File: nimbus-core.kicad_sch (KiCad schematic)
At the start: 0 parts

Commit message: Import shematic
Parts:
- added C1, C11, C13, C15, C16, C17, C18, C20, C21, C23, C24, C25, C4, C6, C7, C9: 100nF, passive:C_0603_Density_Nominal, symbol passive:C0603C104J3RACAUTO
- added C10, C14: 1μF, passive:C_0805_Density_Nominal, symbol passive:C0805C105J3RECAUTO
- added C12: 10μF, passive:C_0805_Density_Nominal, symbol passive:GCM21BR71A106KE22K
- added C19: 4.7μF, passive:C_1206_Density_Nominal, symbol passive:C1206F475K4RACAUTO
- added C2, C3: 10pF, passive:C_0603_Density_Nominal, symbol passive:C0603C100J1GACAUTO
- added C22, C26: 4.7nF, passive:C_0603_Density_Nominal, symbol passive:C0603C472F5GACAUTO
- added C5, C8: 2.2μF, passive:C_0805_Density_Nominal, symbol passive:C0805C225K4RECAUTO
- added D1, D2, D3, D4: ~, diode:D1213A-01T-7, symbol diode:D1213A-01T-7
- added J1: QTE-020-03-L-D-A, connector:QTE-020-03-L-D-A, symbol connector:QTE-020-03-L-D-A
- added J2: QSE-020-01-L-D-A, connector:QSE-020-01-L-D-A, symbol connector:QSE-020-01-L-D-A
- added J3, J6: 532614006, connector:532614004, symbol connector:532614004
- added J4: USB4105-GF-A-120, connector:USB4105-GF-A-120, symbol connector:USB4105-GF-A-120
- added J5: 532614006, connector:532614006, symbol connector:532614006
- added R1, R10, R11, R17, R18, R2, R5, R6, R7, R8, R9: 10kΩ, passive:R_0603_Density_Nominal, symbol passive:CRCW060310K0FKEAHP
- added R12, R13: 0Ω, passive:R_0603_Density_Nominal, symbol passive:CRCW06030000Z0EA
- added R14, R15, R26, R27: 60.4Ω, passive:R_0603_Density_Nominal, symbol passive:CRCW060360R4FKEAHP
- added R16: 10kΩ, passive:C_0603_Density_Nominal, symbol passive:CRCW060310K0FKEAHP
- added R19, R20: 1.8kΩ, passive:R_0603_Density_Nominal, symbol passive:CRCW06031K80FKEAHP
- added R21: 100Ω, passive:R_0603_Density_Nominal, symbol passive:CRCW0603100RFKEA
- added R22, R25: 5.1kΩ, passive:R_0603_Density_Nominal, symbol passive:CRCW06035K10FKEAHP
- added R23: 82kΩ, passive:R_0603_Density_Nominal, symbol passive:CRCW060382K0FKEA
- added R24: 33kΩ, passive:R_0603_Density_Nominal, symbol passive:CRCW060333K0FKEAHP
- added R3, R4: 22.1Ω, passive:R_0603_Density_Nominal, symbol passive:CRCW060322R1FKEA
- added U1: ${MANUFACTURER PART NUMBER}, ic:STM32F405VGT7, symbol ic:STM32F405VGT7
- added U10: ${COLOR}, diode:TLMY1100-GS15, symbol diode:TLMY1100-GS15
- added U4: SN65HVD233-Q1, ic:SN65HVD233-Q1, symbol ic:SN65HVD233-Q1
- added U8: SN65HVD1782-Q1, ic:SN65HVD1782-Q1, symbol ic:SN65HVD1782-Q1
- added U9: USBLC6-2P6, diode:USBLC6-2P6, symbol diode:USBLC6-2P6
- added Y1: 25MHz, passive:ABM11AIG-25.000MHZ-4Z-T3, symbol passive:ABM11AIG-25.000MHZ-4Z-T3
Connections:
- new net: R3.2, U4.4 (RXD)
- new net: R11.2, R13.1, U4.8 (RS)
- new net: C22.1, R14.2, R15.1
- new net: C26.1, R26.2, R27.1
- new net: R12.2, U4.5 (LBK)
- new net: R4.2, R5.2, U4.1 (TXD)
- new net: R21.2, U10.2
- new net +3.3V: C10.1, C11.1, C12.1, C13.1, C14.1, C15.1, C16.1, C17.1, C18.1, C19.1, C23.1, C4.1, C6.1, C7.1, C9.1, J3.1, J5.1, J6.1, R10.1, R11.1, R16.1, R17.1, R19.1, R2.1, R20.1, R5.1, R6.1, R7.1, R8.1, R9.1, U1.100 (VDD), U1.11 (VDD), U1.19 (VDD), U1.21 (VREF+), U1.22 (VDDA), U1.28 (VDD), U1.50 (VDD), U1.6 (VBAT), U1.75 (VDD), U4.3 (VCC), U8.8 (VCC)
- new net ACCEL_IRQ: U1.40 (PE9)
- new net BOOT0: R1.1, U1.94 (BOOT0)
- new net BUZZER: U1.77 (PA15)
- new net CAN1_RX: R3.1, U1.81 (PD0)
- new net CAN1_TX: R4.1, U1.82 (PD1)
- new net CAN_N: C20.1, J3.2, R15.2, U4.6 (CANL)
- new net CAN_P: C21.1, J3.3, R14.1, U4.7 (CANH)
- new net CC1: J4.A5 (CC1), R22.1
- new net CC2: J4.B5 (CC2), R25.1
- new net CHASSIS: J3.MP, J4.SH, J5.MP, J6.MP
- new net FIRE_PYRO1: U1.87 (PD6)
- new net FIRE_PYRO2: U1.86 (PD5)
- new net GND: C1.2, C10.2, C11.2, C12.2, C13.2, C14.2, C15.2, C16.2, C17.2, C18.2, C19.2, C2.2, C20.2, C21.2, C22.2, C23.2, C24.2, C25.2, C26.2, C3.2, C4.2, C5.2, C6.2, C7.2, C8.2, C9.2, D1.2, D2.2, D3.2, D4.2, J1.G1, J1.G2, J1.G3, J1.G4, J2.G1, J2.G2, J2.G3, J2.G4, J3.4, J4.A1 (GND), J4.A12 (GND), J4.B1 (GND), J4.B12 (GND), J5.6, J6.4, R12.1, R13.2, R18.2, R22.2, R23.1, R25.2, U1.10 (VSS), U1.20 (VSSA), U1.27 (VSS), U1.74 (VSS), U1.99 (VSS), U10.1, U4.2 (GND), U8.5 (GND), U9.5 (VBUS), Y1.2, Y1.4
- new net GNSS_RESET: U1.24 (PA1)
- new net GNSS_SAFEBOOT: U1.23 (PA0)
- new net GNSS_TIMEPULSE: U1.25 (PA2)
- new net I2C1_SCL: R19.2, U1.92 (PB6)
- new net I2C1_SDA: R20.2, U1.93 (PB7)
- new net IMU_IRQ: U1.38 (PE7)
- new net OSC_IN: C2.1, U1.12 (PH0), Y1.1
- new net OSC_OUT: C3.1, U1.13 (PH1), Y1.3
- new net PWR_ALERT: U1.95 (PB8)
- new net RADIO_ANT_EN: U1.52 (PB13)
- new net RADIO_BUSY: U1.47 (PB10)
- new net RADIO_IRQ: U1.48 (PB11)
- new net RADIO_RESET: U1.51 (PB12)
- new net RS-485+: C24.1, J6.2, R27.2, U8.6 (A)
- new net RS-485-: C25.1, J6.3, R26.1, U8.7 (B)
- new net RS-485_DIR: R18.1, U1.80 (PC12), U8.2 (~{RE}), U8.3 (DE)
- new net SENSE_PYRO1: U1.36 (PB1)
- new net SENSE_PYRO2: U1.35 (PB0)
- new net SP1_MISO: U1.31 (PA6)
- new net SP1_MOSI: U1.32 (PA7)
- new net SP1_SCK: U1.30 (PA5)
- new net STATUS_LED: R21.1, U1.67 (PA8)
- new net SWCLK: D3.1, J5.4, U1.76 (PA14)
- new net SWDIO: D4.1, J5.5, U1.72 (PA13)
- new net SWO: D2.1, J5.3, U1.89 (PB3)
- new net USART3_RX: R16.2, U1.79 (PC11), U8.1 (R)
- new net USART3_TX: U1.78 (PC10), U8.4 (D)
- new net USB_CONN_D+: J4.A6 (DP1), J4.B6 (DP2), U9.3 (I/O2)
- new net USB_CONN_D-: J4.A7 (DN1), J4.B7 (DN2), U9.1 (I/O1)
- new net USB_D+: U1.71 (PA12), U9.4 (I/O2)
- new net USB_D-: U1.70 (PA11), U9.6 (I/O1)
- new net USB_VBUS: R23.2, R24.1, U1.68 (PA9)
- new net VCAP_1: C8.1, U1.49 (VCAP_1)
- new net VCAP_2: C5.1, U1.73 (VCAP_2)
- new net VUSB: J4.A4 (VBUS), J4.A9 (VBUS), J4.B4 (VBUS), J4.B9 (VBUS), R24.2, U9.2 (GND)
- new net ~{ACCEL_SS}: R2.2, U1.39 (PE8)
- new net ~{BAR_SS}: R6.2, U1.42 (PE11)
- new net ~{GNSS_SS}: R17.2, U1.26 (PA3)
- new net ~{IMU_SS}: R7.2, U1.43 (PE12)
- new net ~{MAG_SS}: R8.2, U1.44 (PE13)
- new net ~{MCU_RESET}: C1.1, D1.1, J5.2, U1.14 (NRST)
- new net ~{MEM_SS}: R9.2, U1.45 (PE14)
- new net ~{RADIO_SS}: R10.2, U1.46 (PE15)
- no-connect marks 0 -> 123

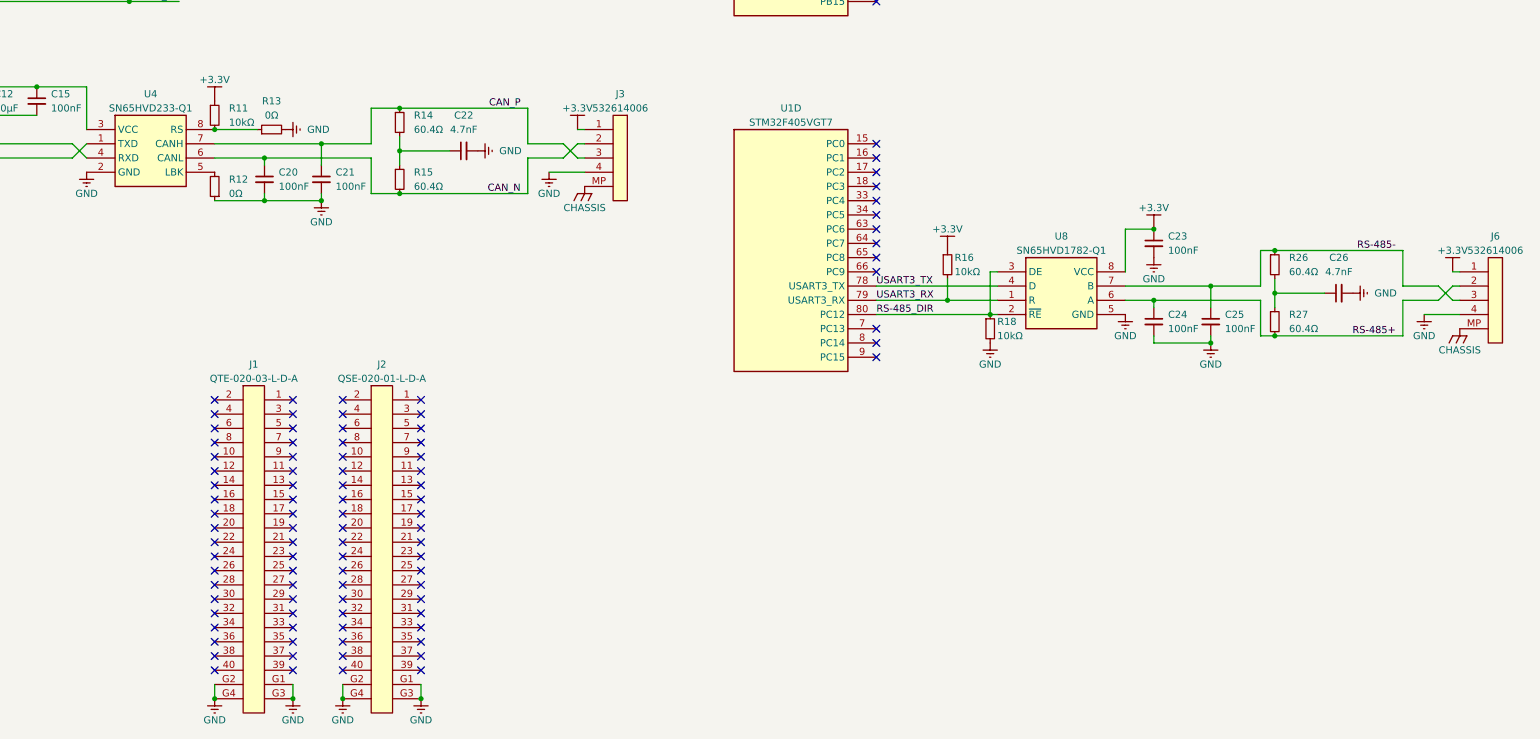
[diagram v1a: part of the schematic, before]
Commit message: Connect bottom passthrough connector with top one both in schematic and PCB
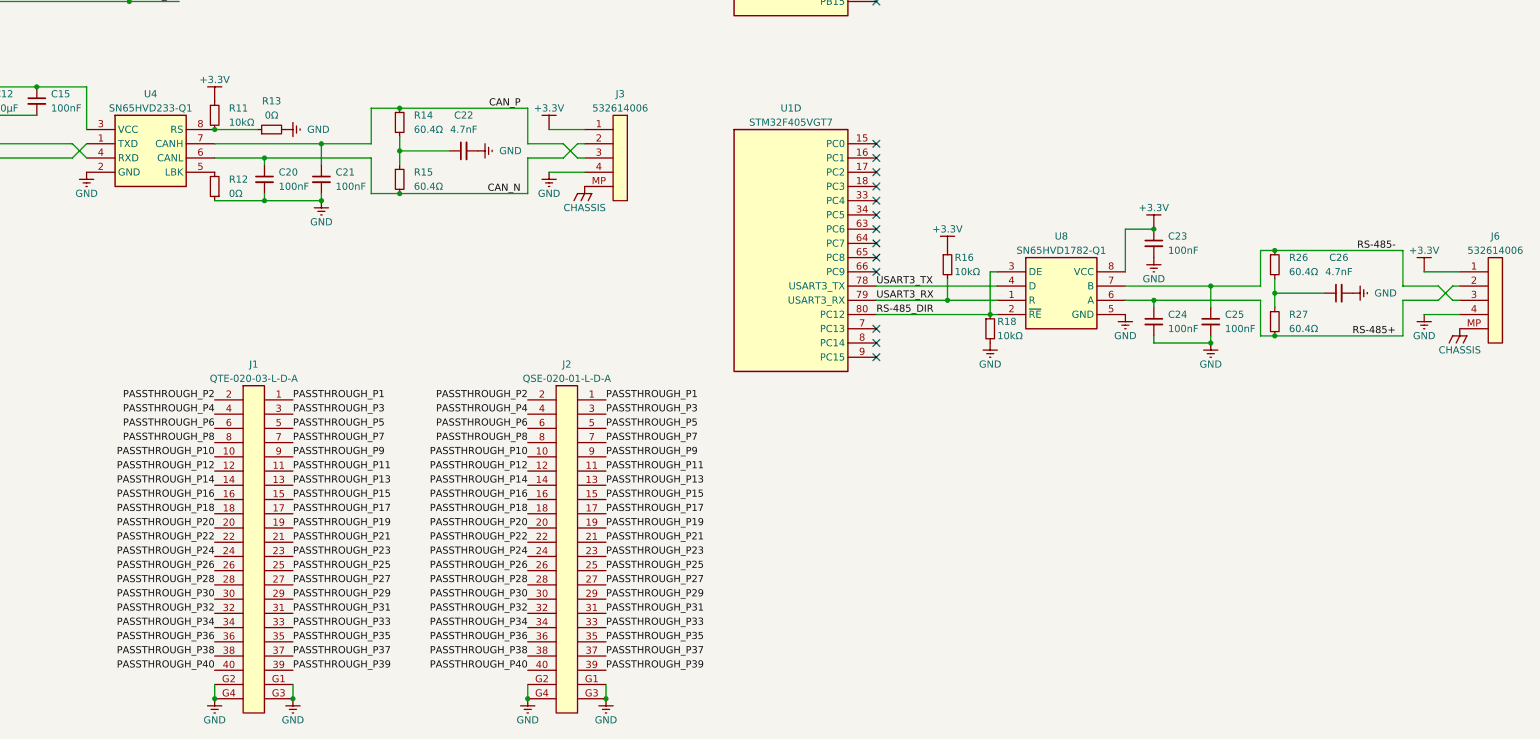
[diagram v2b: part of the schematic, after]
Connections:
- net PASSTHROUGH_P1: now reaches J1.1
- net PASSTHROUGH_P1: now also J2.1
- net PASSTHROUGH_P10: now reaches J1.10
- net PASSTHROUGH_P10: now also J2.10
- net PASSTHROUGH_P11: now reaches J1.11
- net PASSTHROUGH_P11: now also J2.11
- net PASSTHROUGH_P12: now reaches J1.12
- net PASSTHROUGH_P12: now also J2.12
- net PASSTHROUGH_P13: now reaches J1.13
- net PASSTHROUGH_P13: now also J2.13
- net PASSTHROUGH_P14: now reaches J1.14
- net PASSTHROUGH_P14: now also J2.14
- net PASSTHROUGH_P15: now reaches J1.15
- net PASSTHROUGH_P15: now also J2.15
- net PASSTHROUGH_P16: now reaches J1.16
- net PASSTHROUGH_P16: now also J2.16
- net PASSTHROUGH_P17: now reaches J1.17
- net PASSTHROUGH_P17: now also J2.17
- net PASSTHROUGH_P18: now reaches J1.18
- net PASSTHROUGH_P18: now also J2.18
- net PASSTHROUGH_P19: now reaches J1.19
- net PASSTHROUGH_P19: now also J2.19
- net PASSTHROUGH_P2: now reaches J1.2
- net PASSTHROUGH_P2: now also J2.2
- net PASSTHROUGH_P20: now reaches J1.20
- net PASSTHROUGH_P20: now also J2.20
- net PASSTHROUGH_P21: now reaches J1.21
- net PASSTHROUGH_P21: now also J2.21
- net PASSTHROUGH_P22: now reaches J1.22
- net PASSTHROUGH_P22: now also J2.22
- net PASSTHROUGH_P23: now reaches J1.23
- net PASSTHROUGH_P23: now also J2.23
- net PASSTHROUGH_P24: now reaches J1.24
- net PASSTHROUGH_P24: now also J2.24
- net PASSTHROUGH_P25: now reaches J1.25
- net PASSTHROUGH_P25: now also J2.25
- net PASSTHROUGH_P26: now reaches J1.26
- net PASSTHROUGH_P26: now also J2.26
- net PASSTHROUGH_P27: now reaches J1.27
- net PASSTHROUGH_P27: now also J2.27
- net PASSTHROUGH_P28: now reaches J1.28
- net PASSTHROUGH_P28: now also J2.28
- net PASSTHROUGH_P29: now reaches J1.29
- net PASSTHROUGH_P29: now also J2.29
- net PASSTHROUGH_P3: now reaches J1.3
- net PASSTHROUGH_P3: now also J2.3
- net PASSTHROUGH_P30: now reaches J1.30
- net PASSTHROUGH_P30: now also J2.30
- net PASSTHROUGH_P31: now reaches J1.31
- net PASSTHROUGH_P31: now also J2.31
- net PASSTHROUGH_P32: now reaches J1.32
- net PASSTHROUGH_P32: now also J2.32
- net PASSTHROUGH_P33: now reaches J1.33
- net PASSTHROUGH_P33: now also J2.33
- net PASSTHROUGH_P34: now reaches J1.34
- net PASSTHROUGH_P34: now also J2.34
- net PASSTHROUGH_P35: now reaches J1.35
- net PASSTHROUGH_P35: now also J2.35
- net PASSTHROUGH_P36: now reaches J1.36
- net PASSTHROUGH_P36: now also J2.36
- net PASSTHROUGH_P37: now reaches J1.37
- net PASSTHROUGH_P37: now also J2.37
- net PASSTHROUGH_P38: now reaches J1.38
- net PASSTHROUGH_P38: now also J2.38
- net PASSTHROUGH_P39: now reaches J1.39
- net PASSTHROUGH_P39: now also J2.39
- net PASSTHROUGH_P4: now reaches J1.4
- net PASSTHROUGH_P4: now also J2.4
- net PASSTHROUGH_P40: now reaches J1.40
- net PASSTHROUGH_P40: now also J2.40
- net PASSTHROUGH_P5: now reaches J1.5
- net PASSTHROUGH_P5: now also J2.5
- net PASSTHROUGH_P6: now reaches J1.6
- net PASSTHROUGH_P6: now also J2.6
- net PASSTHROUGH_P7: now reaches J1.7
- net PASSTHROUGH_P7: now also J2.7
- net PASSTHROUGH_P8: now reaches J1.8
- net PASSTHROUGH_P8: now also J2.8
- net PASSTHROUGH_P9: now reaches J1.9
- net PASSTHROUGH_P9: now also J2.9
- no-connect marks 123 -> 43
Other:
- moved on the sheet: J2

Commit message: Add first connections to passtrough, will likely need some iteration
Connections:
- net PASSTHROUGH_P20 is gone; now on net ACCEL_IRQ: J1.20, J2.20
- net PASSTHROUGH_P24 is gone; now on net IMU_IRQ: J1.24, J2.24
- net RADIO_BUSY is gone; now on net PASSTHROUGH_P6: U1.47 (PB10)
- net RADIO_IRQ is gone; now on net PASSTHROUGH_P4: U1.48 (PB11)
- net SENSE_PYRO1 is gone; now on net PASSTHROUGH_P28: U1.36 (PB1)
- net SENSE_PYRO2 is gone; now on net PASSTHROUGH_P30: U1.35 (PB0)
- net SP1_MISO is gone; now on net PASSTHROUGH_P38: U1.31 (PA6)
- net SP1_MOSI is gone; now on net PASSTHROUGH_P36: U1.32 (PA7)
- net SP1_SCK is gone; now on net PASSTHROUGH_P40: U1.30 (PA5)
- net ~{ACCEL_SS} is gone; now on net PASSTHROUGH_P22: R2.2, U1.39 (PE8)
- net ~{BAR_SS} is gone; now on net PASSTHROUGH_P16: R6.2, U1.42 (PE11)
- net ~{IMU_SS} is gone; now on net PASSTHROUGH_P14: R7.2, U1.43 (PE12)
- net ~{MAG_SS} is gone; now on net PASSTHROUGH_P12: R8.2, U1.44 (PE13)
- net ~{MEM_SS} is gone; now on net PASSTHROUGH_P10: R9.2, U1.45 (PE14)
- net ~{RADIO_SS} is gone; now on net PASSTHROUGH_P8: R10.2, U1.46 (PE15)
- net PASSTHROUGH_P18: now also U1.41 (PE10)
- net PASSTHROUGH_P26: now also U1.37 (PB2)
- net PASSTHROUGH_P32: now also U1.34 (PC5)
- net PASSTHROUGH_P34: now also U1.33 (PC4)
- no-connect marks 43 -> 39
